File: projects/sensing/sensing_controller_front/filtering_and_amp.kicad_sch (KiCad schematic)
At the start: 26 parts, among them U4 AD8630

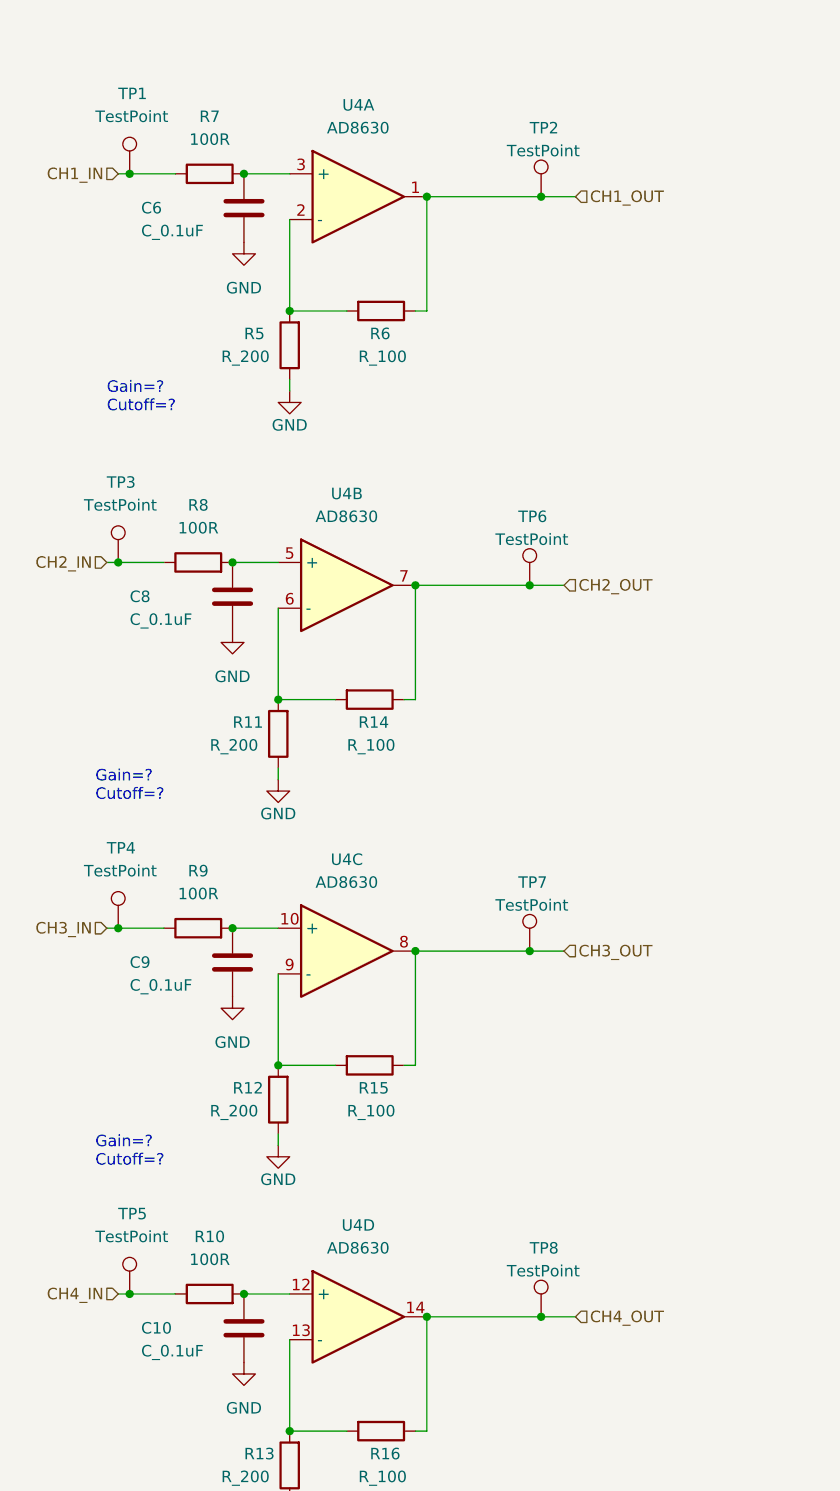
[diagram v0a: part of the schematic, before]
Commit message: changing order of CH_INs and CH_OUTs for ease of layout
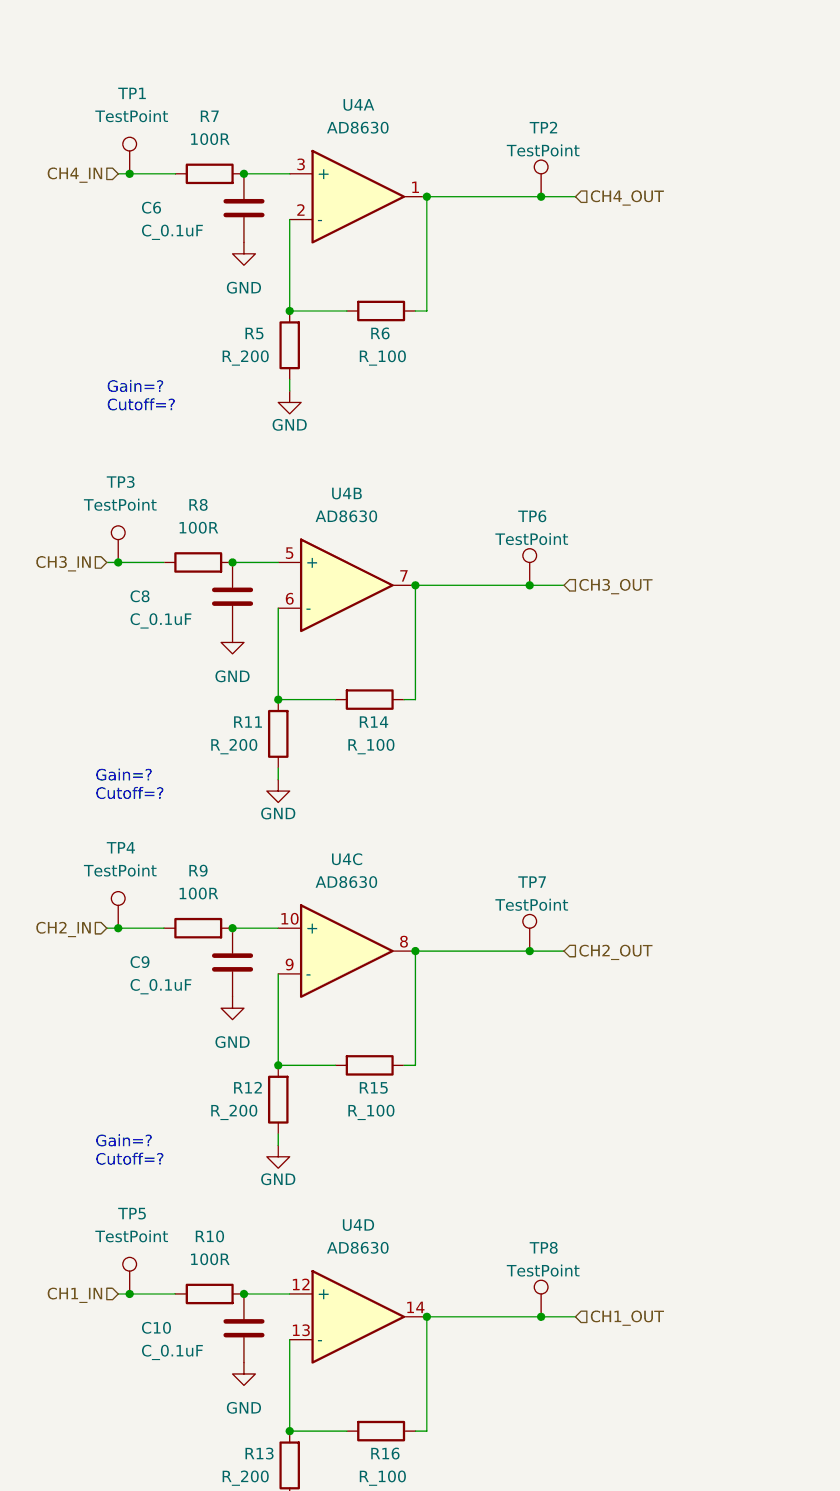
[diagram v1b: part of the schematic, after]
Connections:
- net CH1_IN: now also R10.1, TP5.1; no longer R7.1, TP1.1
- net CH1_OUT: now also R16.1, TP8.1, U4.14; no longer R6.1, TP2.1, U4.1
- net CH2_IN: now also R9.1, TP4.1; no longer R8.1, TP3.1
- net CH2_OUT: now also R15.1, TP7.1, U4.8; no longer R14.1, TP6.1, U4.7
- net CH3_IN: now also R8.1, TP3.1; no longer R9.1, TP4.1
- net CH3_OUT: now also R14.1, TP6.1, U4.7; no longer R15.1, TP7.1, U4.8
- net CH4_IN: now also R7.1, TP1.1; no longer R10.1, TP5.1
- net CH4_OUT: now also R6.1, TP2.1, U4.1; no longer R16.1, TP8.1, U4.14
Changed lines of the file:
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@@
     (effects (font (size 1.27 1.27)) (justify left bottom))
   )
-  (hierarchical_label "CH2_OUT" (shape input) (at 83.82 85.09 0)
+  (hierarchical_label "CH3_OUT" (shape input) (at 83.82 85.09 0)
     (effects (font (size 1.27 1.27)) (justify left))
   )
-  (hierarchical_label "CH3_IN" (shape input) (at 33.02 123.19 180)
+  (hierarchical_label "CH2_IN" (shape input) (at 33.02 123.19 180)
     (effects (font (size 1.27 1.27)) (justify right))
   )
-  (hierarchical_label "CH1_IN" (shape input) (at 34.29 39.37 180)
+  (hierarchical_label "CH4_IN" (shape input) (at 34.29 39.37 180)
     (effects (font (size 1.27 1.27)) (justify right))
   )
-  (hierarchical_label "CH1_OUT" (shape input) (at 85.09 41.91 0)
+  (hierarchical_label "CH4_OUT" (shape input) (at 85.09 41.91 0)
     (effects (font (size 1.27 1.27)) (justify left))
   )
-  (hierarchical_label "CH3_OUT" (shape input) (at 83.82 125.73 0)
+  (hierarchical_label "CH2_OUT" (shape input) (at 83.82 125.73 0)
     (effects (font (size 1.27 1.27)) (justify left))
   )
-  (hierarchical_label "CH4_IN" (shape input) (at 34.29 163.83 180)
+  (hierarchical_label "CH1_IN" (shape input) (at 34.29 163.83 180)
     (effects (font (size 1.27 1.27)) (justify right))
   )
-  (hierarchical_label "CH4_OUT" (shape input) (at 85.09 166.37 0)
+  (hierarchical_label "CH1_OUT" (shape input) (at 85.09 166.37 0)
     (effects (font (size 1.27 1.27)) (justify left))
   )
-  (hierarchical_label "CH2_IN" (shape input) (at 33.02 82.55 180)
+  (hierarchical_label "CH3_IN" (shape input) (at 33.02 82.55 180)
     (effects (font (size 1.27 1.27)) (justify right))
   )

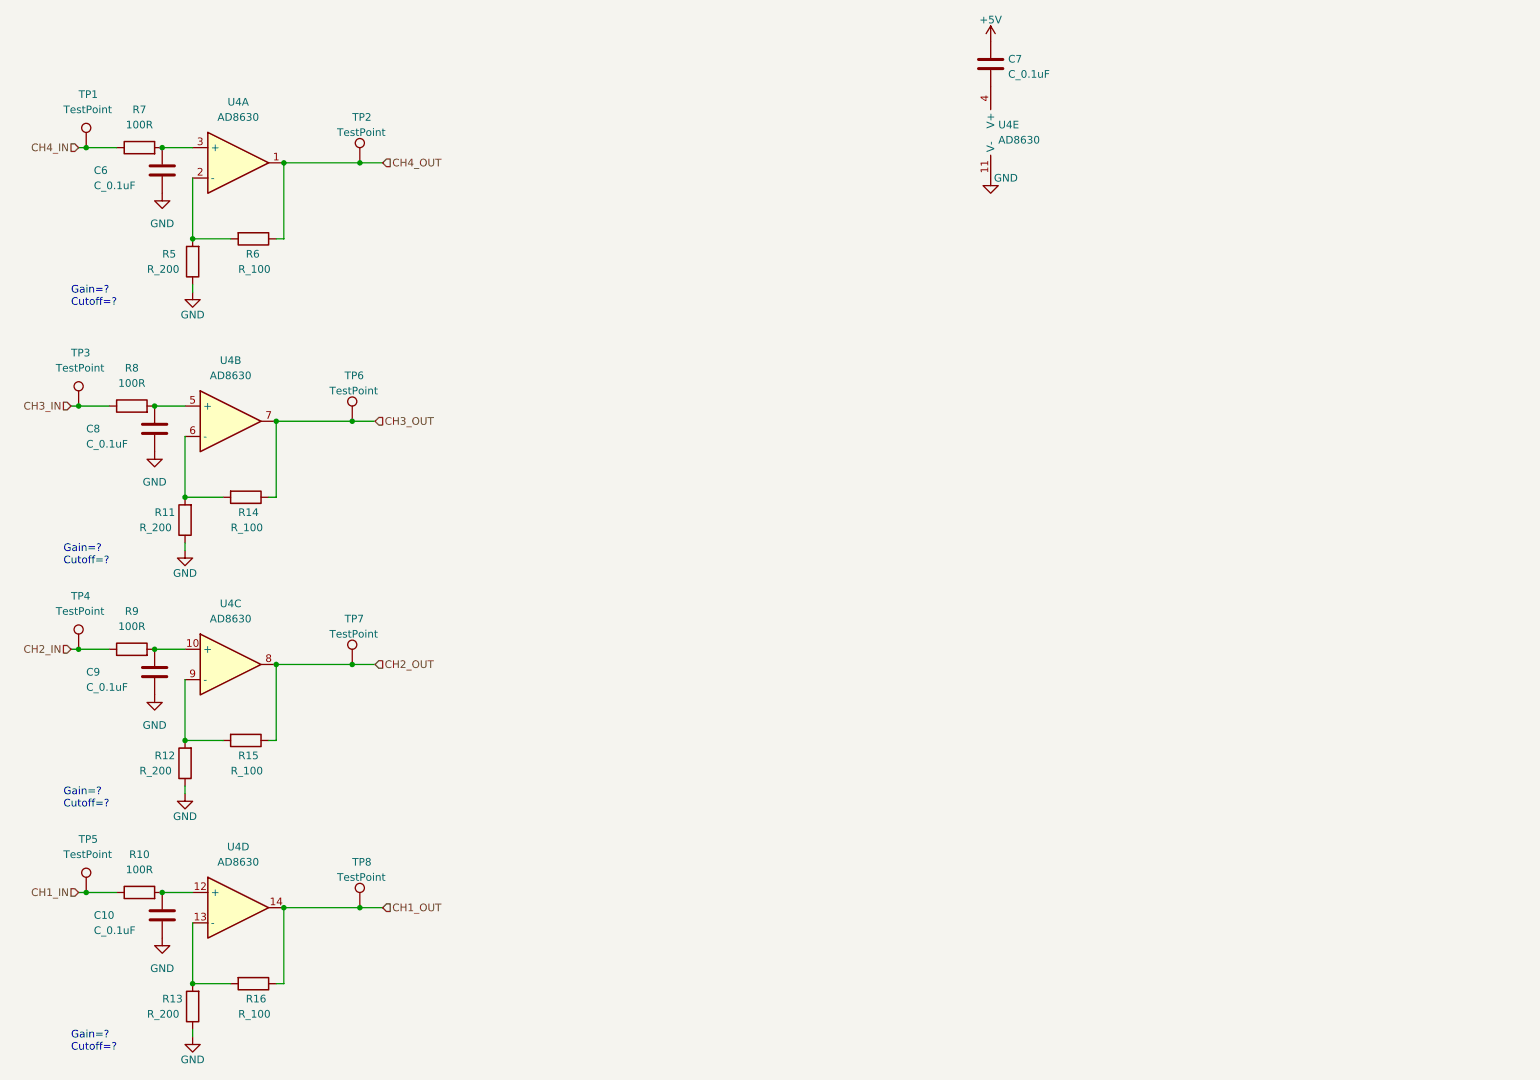
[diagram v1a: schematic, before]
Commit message: added gain + cutoff values
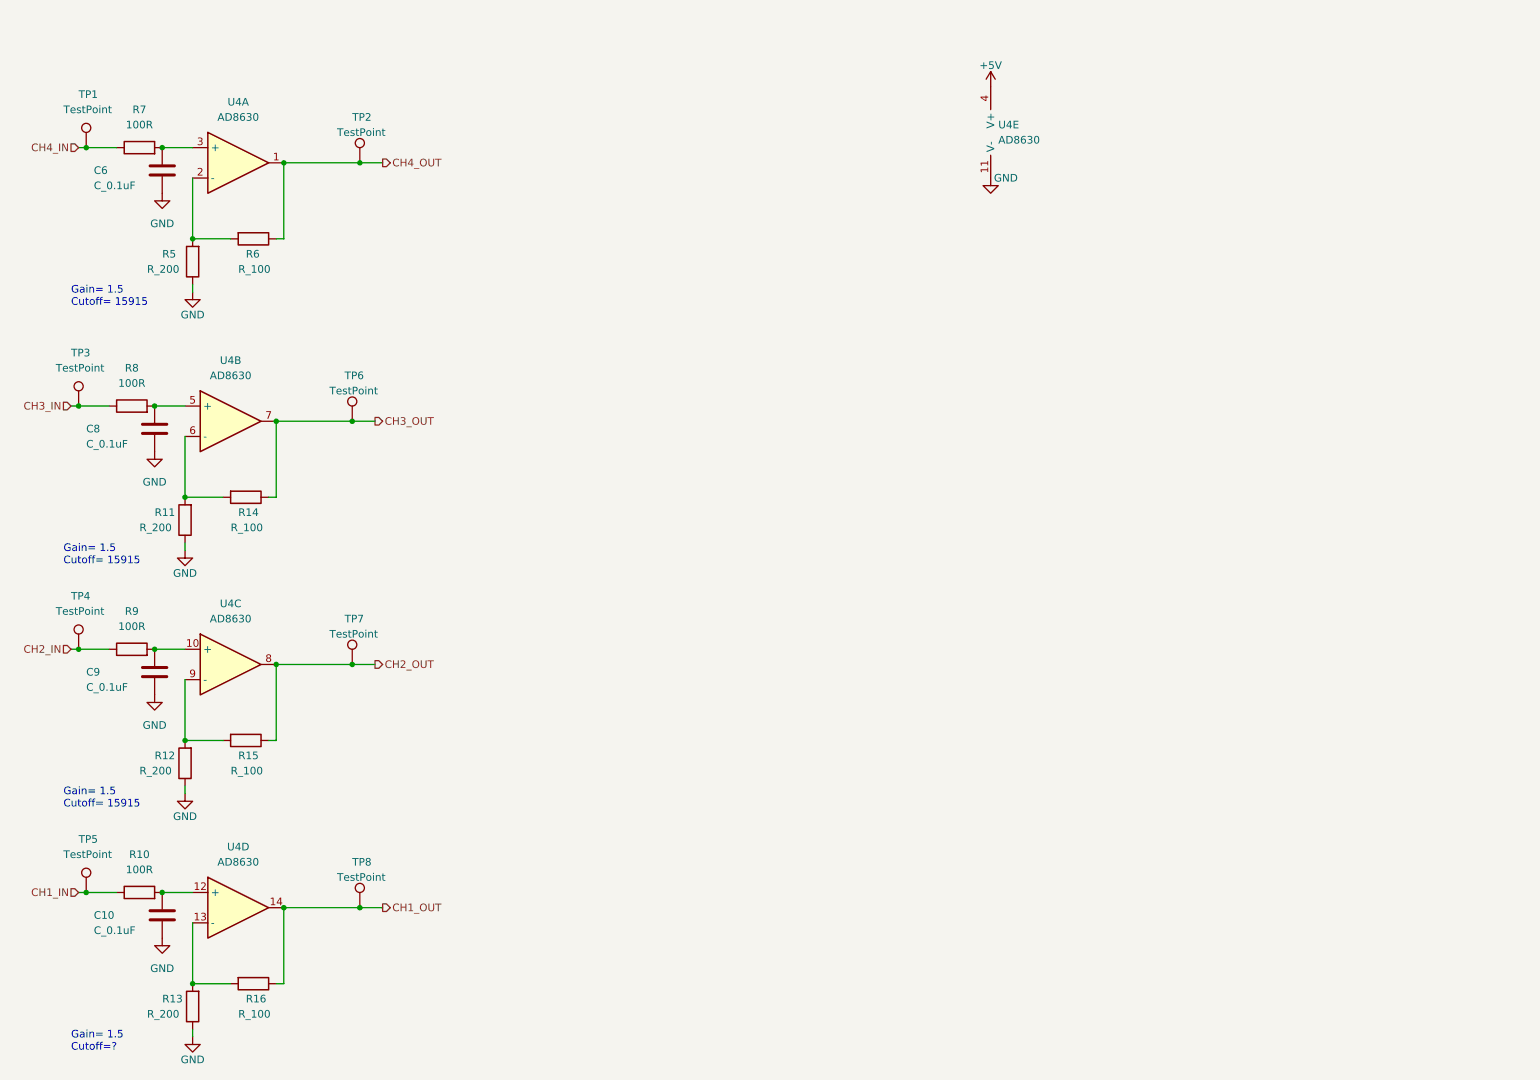
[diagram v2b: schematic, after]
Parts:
- removed C7: C_0.1uF, OEM:C_0603, symbol formula:C_0.1uF
- TP2: footprint (none) -> TestPoint:TestPoint_Pad_D2.0mm
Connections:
- net +5V: now also U4.4 (V+)
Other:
- note added: "Gain= 1.5 Cutoff= 15915"
- note added: "Gain= 1.5 Cutoff=?"
- note removed: "Gain=? Cutoff=?"
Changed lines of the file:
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@@
     (stroke (width 0) (type default) (color 0 0 0 0))
   )
-  (text "Gain=?\nCutoff=?" (at 33.02 66.04 0)
+  (text "Gain= 1.5\nCutoff= 15915" (at 33.02 66.04 0)
     (effects (font (size 1.27 1.27)) (justify left bottom))
   )
-  (text "Gain=?\nCutoff=?" (at 31.75 109.22 0)
+  (text "Gain= 1.5\nCutoff= 15915" (at 31.75 109.22 0)
     (effects (font (size 1.27 1.27)) (justify left bottom))
   )
-  (text "Gain=?\nCutoff=?" (at 33.02 190.5 0)
+  (text "Gain= 1.5\nCutoff=?" (at 33.02 190.5 0)
     (effects (font (size 1.27 1.27)) (justify left bottom))
   )
-  (text "Gain=?\nCutoff=?" (at 31.75 149.86 0)
+  (text "Gain= 1.5\nCutoff= 15915" (at 31.75 149.86 0)
     (effects (font (size 1.27 1.27)) (justify left bottom))
   )
-  (hierarchical_label "CH3_OUT" (shape input) (at 83.82 85.09 0)
+  (hierarchical_label "CH3_OUT" (shape output) (at 83.82 85.09 0)
     (effects (font (size 1.27 1.27)) (justify left))
   )
@@
     (effects (font (size 1.27 1.27)) (justify right))
   )
-  (hierarchical_label "CH4_OUT" (shape input) (at 85.09 41.91 0)
+  (hierarchical_label "CH4_OUT" (shape output) (at 85.09 41.91 0)
     (effects (font (size 1.27 1.27)) (justify left))
   )
-  (hierarchical_label "CH2_OUT" (shape input) (at 83.82 125.73 0)
+  (hierarchical_label "CH2_OUT" (shape output) (at 83.82 125.73 0)
     (effects (font (size 1.27 1.27)) (justify left))
   )
@@
     (effects (font (size 1.27 1.27)) (justify right))
   )
-  (hierarchical_label "CH1_OUT" (shape input) (at 85.09 166.37 0)
+  (hierarchical_label "CH1_OUT" (shape output) (at 85.09 166.37 0)
     (effects (font (size 1.27 1.27)) (justify left))
   )
@@
       (effects (font (size 1.27 1.27)) (justify left))
     )
-    (property "Footprint" "" (id 2) (at 86.36 41.91 0)
+    (property "Footprint" "TestPoint:TestPoint_Pad_D2.0mm" (id 2) (at 86.36 41.91 0)
       (effects (font (size 1.27 1.27)) hide)
     )
@@
     (pin "1")
   )
-  (symbol (lib_id "formula:C_0.1uF") (at 186.69 25.4 0) (unit 1)
-    (in_bom yes) (on_board yes) (fields_autoplaced)
-    (property "Reference" "C7" (id 0) (at 189.611 24.5653 0)
-      (effects (font (size 1.27 1.27)) (justify left))
-    )
-    (property "Value" "C_0.1uF" (id 1) (at 189.611 27.1022 0)
-      (effects (font (size 1.27 1.27)) (justify left))
-    )
-    (property "Footprint" "OEM:C_0603" (id 2) (at 187.6552 29.21 0)
-      (effects (font (size 1.27 1.27)) hide)
-    )
-    (property "Datasheet" "http://datasheets.avx.com/X7RDielectric.pdf" (id 3) (at 187.325 22.86 0)
-      (effects (font (size 1.27 1.27)) hide)
-    )
-    (property "MFN" "DK" (id 4) (at 186.69 25.4 0)
-      (effects (font (size 1.524 1.524)) hide)
-    )
-    (property "MPN" "478-3352-1-ND" (id 5) (at 186.69 25.4 0)
-      (effects (font (size 1.524 1.524)) hide)
-    )
-    (property "PurchasingLink" "https://www.digikey.com/products/en?keywords=478-3352-1-ND" (id 6) (at 197.485 12.7 0)
-      (effects (font (size 1.524 1.524)) hide)
-    )
-    (pin "1")
-    (pin "2")
-  )
   (symbol (lib_id "formula:C_0.1uF") (at 48.26 43.18 0) (unit 1)
     (in_bom yes) (on_board yes)
@@
     (pin "1")
   )
-  (symbol (lib_id "power:+5V") (at 186.69 21.59 0) (unit 1)
-    (in_bom yes) (on_board yes) (fields_autoplaced)
-    (property "Reference" "#PWR?" (id 0) (at 186.69 25.4 0)
-      (effects (font (size 1.27 1.27)) hide)
-    )
-    (property "Value" "+5V" (id 1) (at 186.69 18.0142 0))
-    (property "Footprint" "" (id 2) (at 186.69 21.59 0)
-      (effects (font (size 1.27 1.27)) hide)
-    )
-    (property "Datasheet" "" (id 3) (at 186.69 21.59 0)
+  (symbol (lib_id "power:+5V") (at 186.69 29.21 0) (unit 1)
+    (in_bom yes) (on_board yes) (fields_autoplaced)
+    (property "Reference" "#PWR?" (id 0) (at 186.69 33.02 0)
+      (effects (font (size 1.27 1.27)) hide)
+    )
+    (property "Value" "+5V" (id 1) (at 186.69 25.6342 0))
+    (property "Footprint" "" (id 2) (at 186.69 29.21 0)
+      (effects (font (size 1.27 1.27)) hide)
+    )
+    (property "Datasheet" "" (id 3) (at 186.69 29.21 0)
       (effects (font (size 1.27 1.27)) hide)
     )
@@
   )
   (symbol (lib_name "AD8630_1") (lib_id "formula:AD8630") (at 189.23 36.83 0) (unit 5)
-    (in_bom yes) (on_board yes) (fields_autoplaced)
+    (in_bom yes) (on_board yes)
     (property "Reference" "U4" (id 0) (at 187.96 35.5599 0)
       (effects (font (size 1.27 1.27)) (justify left))

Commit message: removed amplification for wheel-speed sensors
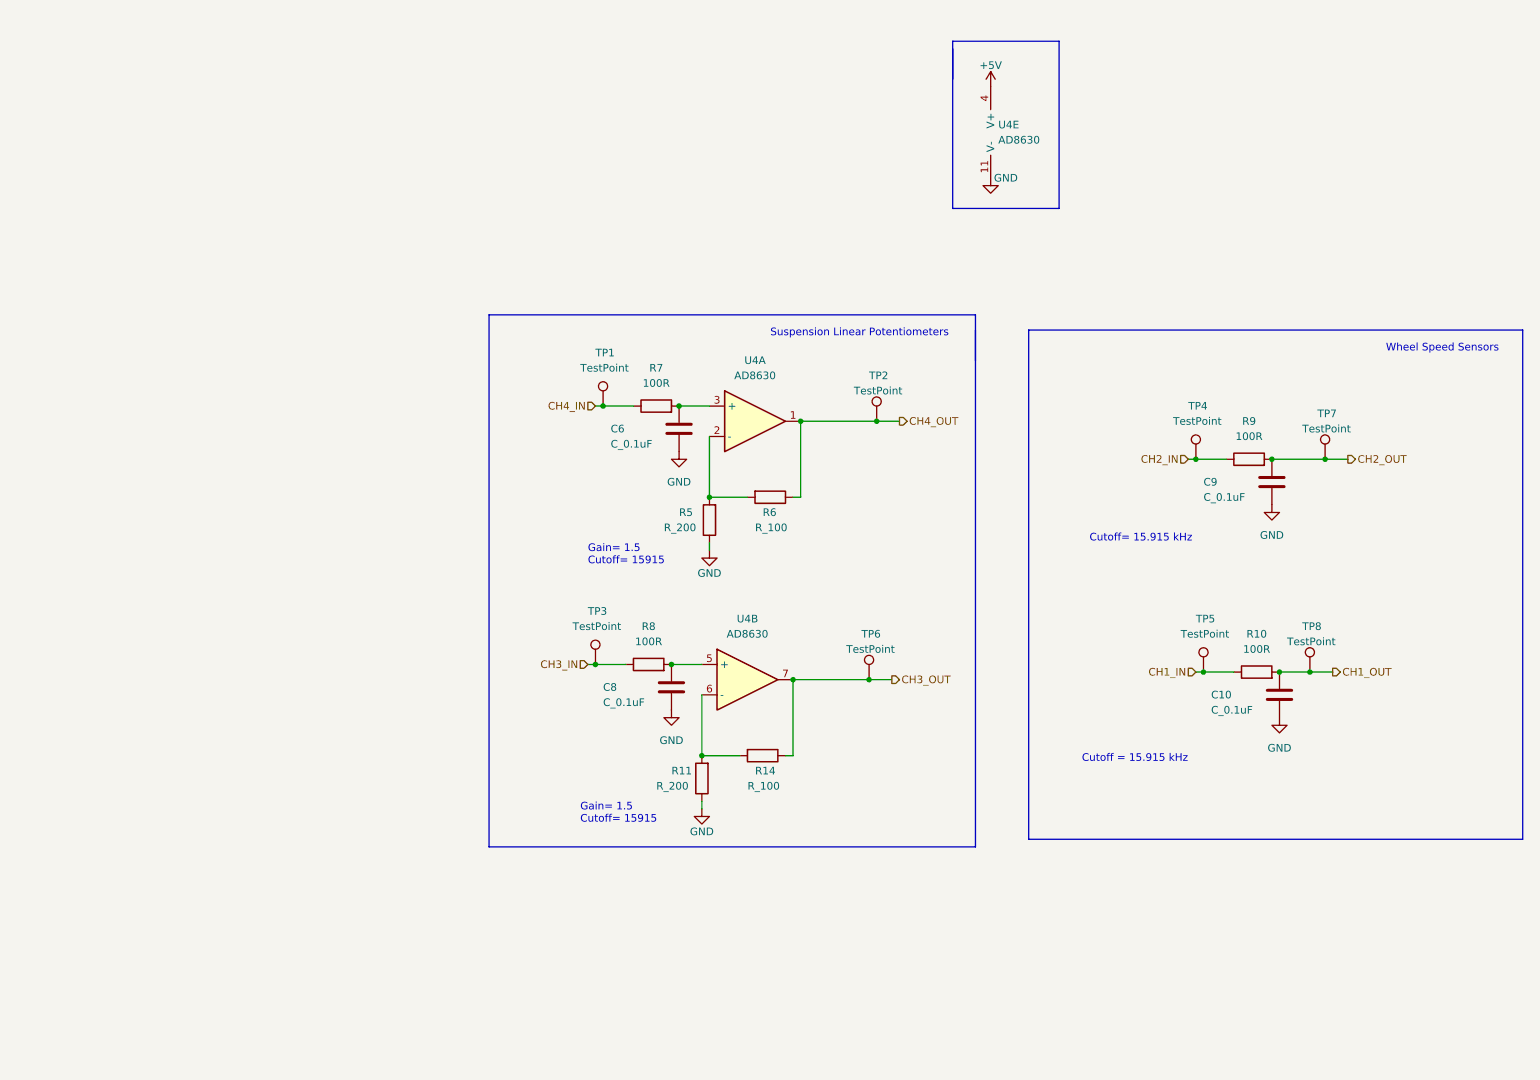
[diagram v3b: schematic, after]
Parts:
- removed R12, R13: R_200, OEM:R_0603, symbol formula:R_200
- removed R15, R16: R_100, OEM:R_0603, symbol formula:R_100
- removed unit 3 of U4
- removed unit 4 of U4
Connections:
- net CH1_OUT: now also C10.1, R10.2
- net CH2_OUT: now also C9.1, R9.2
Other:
- note added: "Cutoff = 15.915 kHz"
- note added: "Cutoff= 15.915 kHz"
- note added: "Suspension Linear Potentiometers"
- note added: "Wheel Speed Sensors"
- note removed: "Gain= 1.5 Cutoff=?"
- moved on the sheet: C10, C6, C8, C9, R10, R11, R14, R5, R6, R7, R8, R9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
